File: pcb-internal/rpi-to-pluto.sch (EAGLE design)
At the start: 7 parts, among them IC1 74HCT00, J1 JST-PH_4-PIN_HEADER

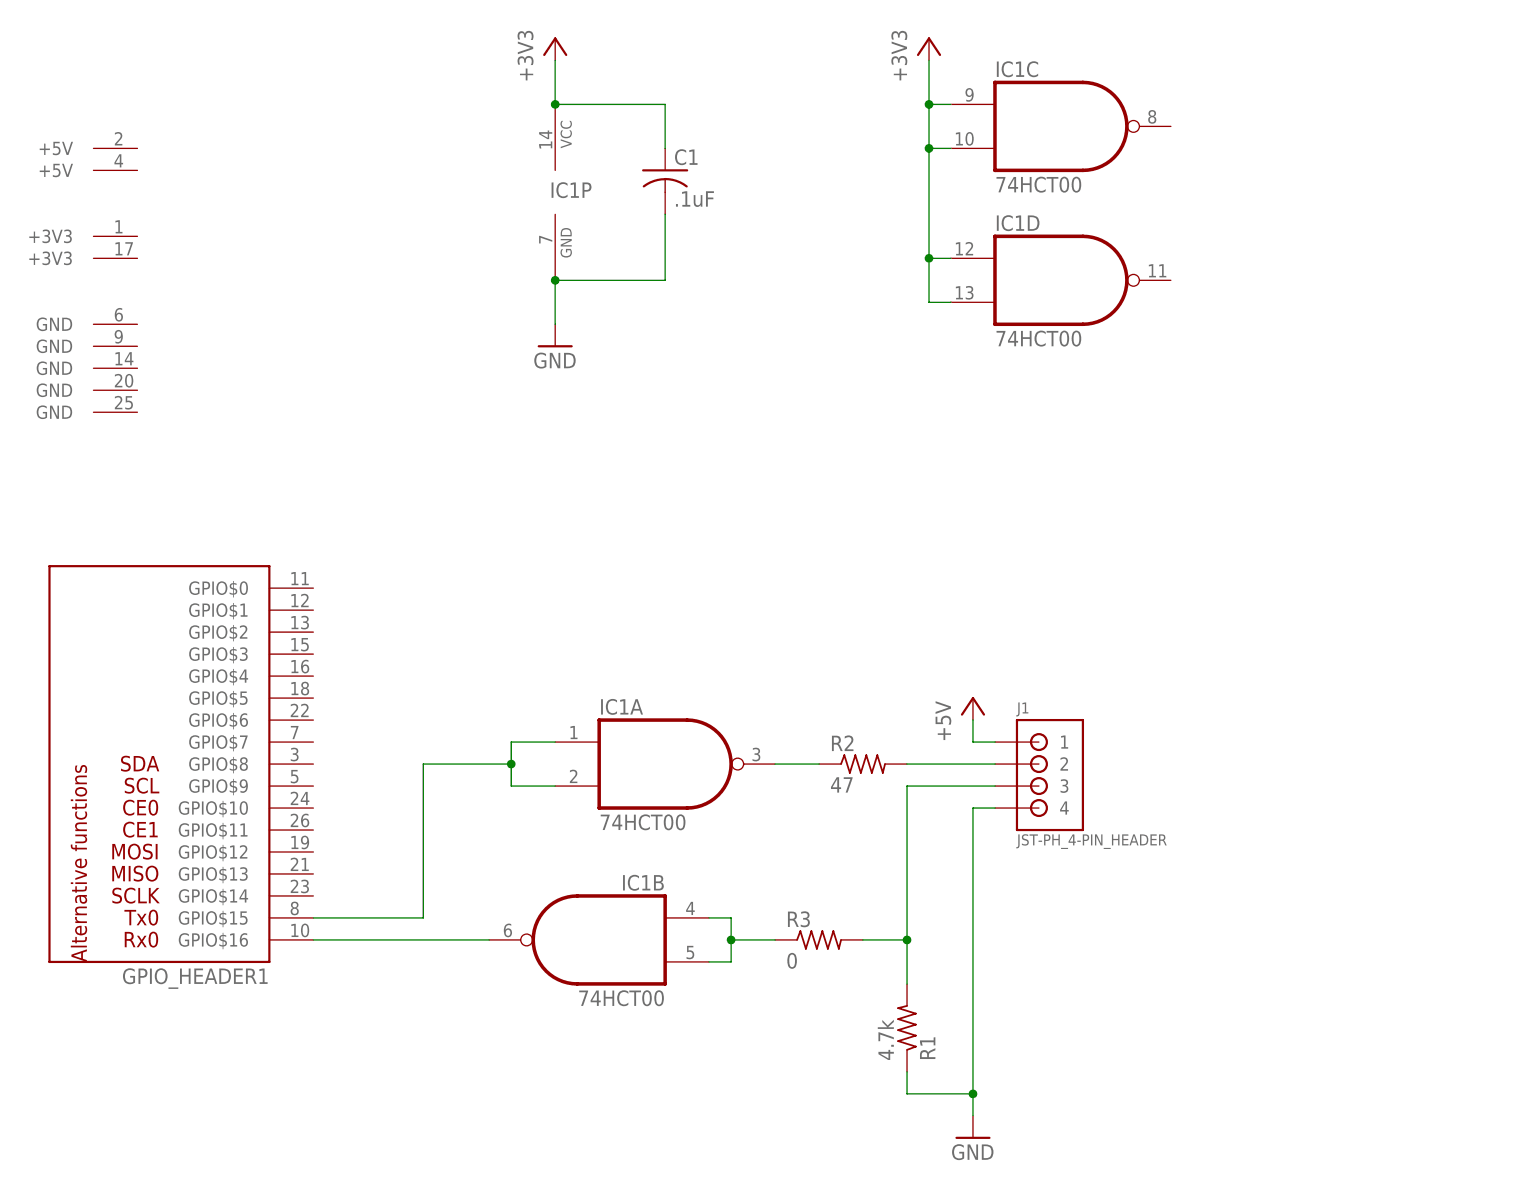
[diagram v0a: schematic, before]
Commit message: New rpi-to-pluto board using the 74LVC2G14
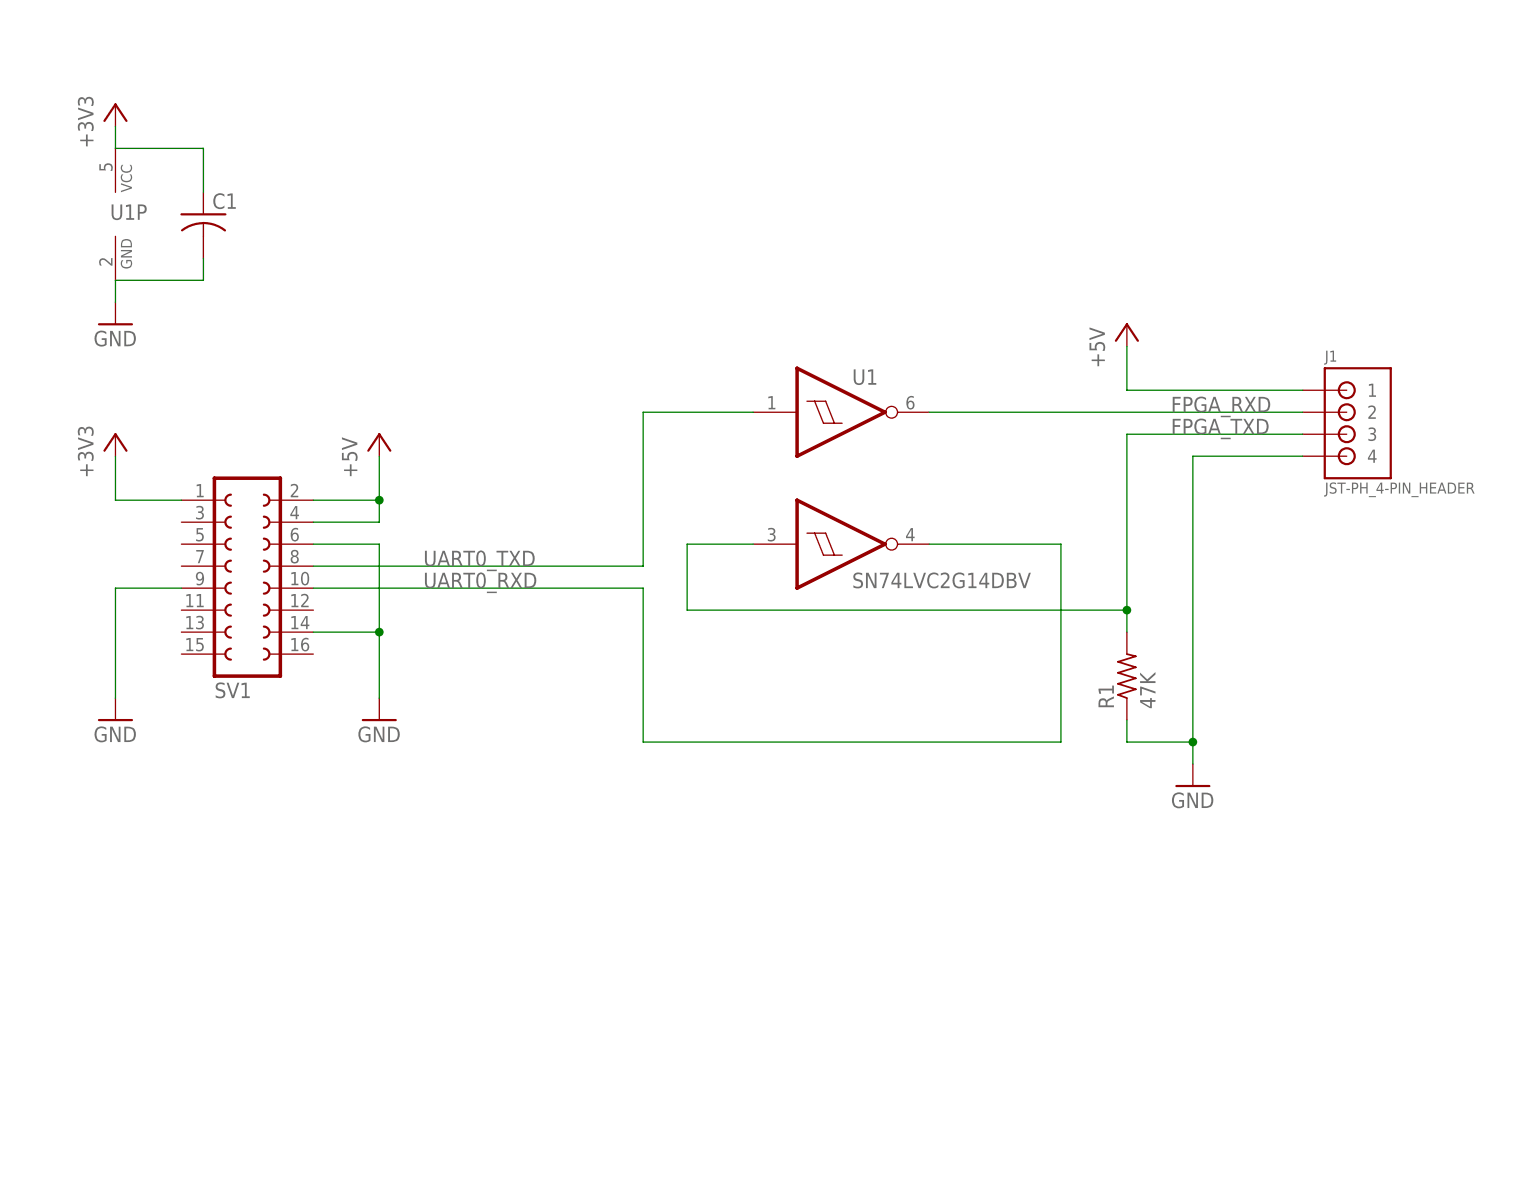
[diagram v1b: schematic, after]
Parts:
- removed GPIO_HEADER1: RPI_GPIO_HEADER, rpi-header:RPI_GPIO_HEADER
- removed IC1: 74HCT00, 74xx-us:7400N
- removed R2: 47, resistor:R-US_0309/12
- removed R3: 0, resistor:R-US_0309/12
- added SV1: (no value), con-lsta:FE08-2
- added U1: SN74LVC2G14DBV, lio:SN74LVC2G14DBV
- C1: value .1uF -> (none); device resistor:C-US050-035X075 -> resistor:C-USC0805
- R1: value 4.7k -> 47K; device resistor:R-US_0309/12 -> resistor:R-US_R0805
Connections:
- removed net N$1: J1.3, R1.2, R3.2
- removed net N$2: IC1A.O, R2.1
- removed net N$3: J1.2, R2.2
- removed net N$4: GPIO_HEADER1G$1.GPIO$15, IC1A.I0, IC1A.I1
- removed net N$5: IC1B.I0, IC1B.I1, R3.1
- removed net N$7: GPIO_HEADER1G$1.GPIO$16, IC1B.O
- new net FPGA_RXD: J1.2, U1Q.1Y
- new net FPGA_TXD: J1.3, R1.2, U1Q.2A
- new net UART0_RXD: SV1.10, U1Q.2Y
- new net UART0_TXD: SV1.8, U1Q.1A
- net +3V3: now also SV1.1, U1P.VCC; no longer IC1C.I0, IC1C.I1, IC1D.I0, IC1D.I1, IC1P.VCC
- net +5V: now also SV1.2, SV1.4
- net GND: now also SV1.14, SV1.6, SV1.9, U1P.GND; no longer IC1P.GND
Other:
- moved on the sheet: C1, J1, R1
